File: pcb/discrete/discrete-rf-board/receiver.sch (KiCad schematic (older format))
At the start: 31 parts, among them U7 MAX1193

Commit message: Autofill
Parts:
- C114, C116: footprint (none) -> Capacitor_SMD:C_0402_1005Metric; Mouser (none) -> 80-C0402C104M4P
- R81, R82, R83, R84: footprint (none) -> Resistor_SMD:R_0402_1005Metric; Mouser (none) -> 603-AC0402FR-1310KL
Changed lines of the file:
@@
 F 0 "R82" H 7580 3870 50  0000 L CNN
 F 1 "10kR" H 7580 3810 50  0000 L CNN
-F 2 "" H 7550 3850 50  0001 C CNN
+F 2 "Resistor_SMD:R_0402_1005Metric" H 7550 3850 50  0001 C CNN
 F 3 "~" H 7550 3850 50  0001 C CNN
+F 4 "603-AC0402FR-1310KL" H 7550 3850 50  0001 C CNN "Mouser"
 	1    7550 3850
 	1    0    0    -1
@@
 F 0 "R84" H 7980 3870 50  0000 L CNN
 F 1 "10kR" H 7980 3810 50  0000 L CNN
-F 2 "" H 7950 3850 50  0001 C CNN
+F 2 "Resistor_SMD:R_0402_1005Metric" H 7950 3850 50  0001 C CNN
 F 3 "~" H 7950 3850 50  0001 C CNN
+F 4 "603-AC0402FR-1310KL" H 7950 3850 50  0001 C CNN "Mouser"
 	1    7950 3850
 	1    0    0    -1
@@
 F 0 "R81" H 7580 2470 50  0000 L CNN
 F 1 "10kR" H 7580 2410 50  0000 L CNN
-F 2 "" H 7550 2450 50  0001 C CNN
+F 2 "Resistor_SMD:R_0402_1005Metric" H 7550 2450 50  0001 C CNN
 F 3 "~" H 7550 2450 50  0001 C CNN
+F 4 "603-AC0402FR-1310KL" H 7550 2450 50  0001 C CNN "Mouser"
 	1    7550 2450
 	1    0    0    -1
@@
 F 0 "R83" H 7980 2470 50  0000 L CNN
 F 1 "10kR" H 7980 2410 50  0000 L CNN
-F 2 "" H 7950 2450 50  0001 C CNN
+F 2 "Resistor_SMD:R_0402_1005Metric" H 7950 2450 50  0001 C CNN
 F 3 "~" H 7950 2450 50  0001 C CNN
+F 4 "603-AC0402FR-1310KL" H 7950 2450 50  0001 C CNN "Mouser"
 	1    7950 2450
 	1    0    0    -1
@@
 F 0 "C116" H 10160 2720 50  0000 L CNN
 F 1 "0.1 uF" H 10160 2570 50  0000 L CNN
-F 2 "" H 10150 2650 50  0001 C CNN
+F 2 "Capacitor_SMD:C_0402_1005Metric" H 10150 2650 50  0001 C CNN
 F 3 "~" H 10150 2650 50  0001 C CNN
+F 4 "80-C0402C104M4P" H 10150 2650 50  0001 C CNN "Mouser"
 	1    10150 2650
 	1    0    0    -1
@@
 F 0 "C114" H 9160 2720 50  0000 L CNN
 F 1 "0.1 uF" H 9160 2570 50  0000 L CNN
-F 2 "" H 9150 2650 50  0001 C CNN
+F 2 "Capacitor_SMD:C_0402_1005Metric" H 9150 2650 50  0001 C CNN
 F 3 "~" H 9150 2650 50  0001 C CNN
+F 4 "80-C0402C104M4P" H 9150 2650 50  0001 C CNN "Mouser"
 	1    9150 2650
 	1    0    0    -1

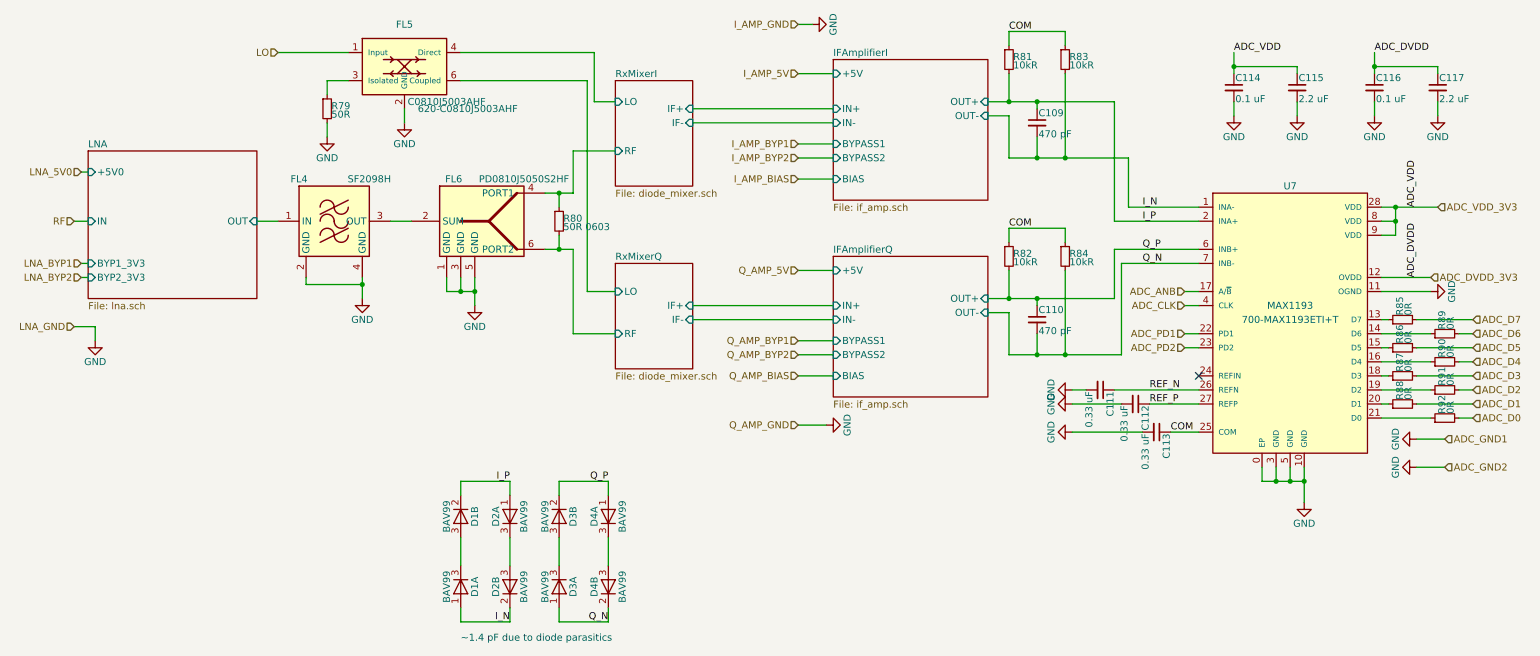
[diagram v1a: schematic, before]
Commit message: Reannotate everything; I'm trying to cut down the number of components
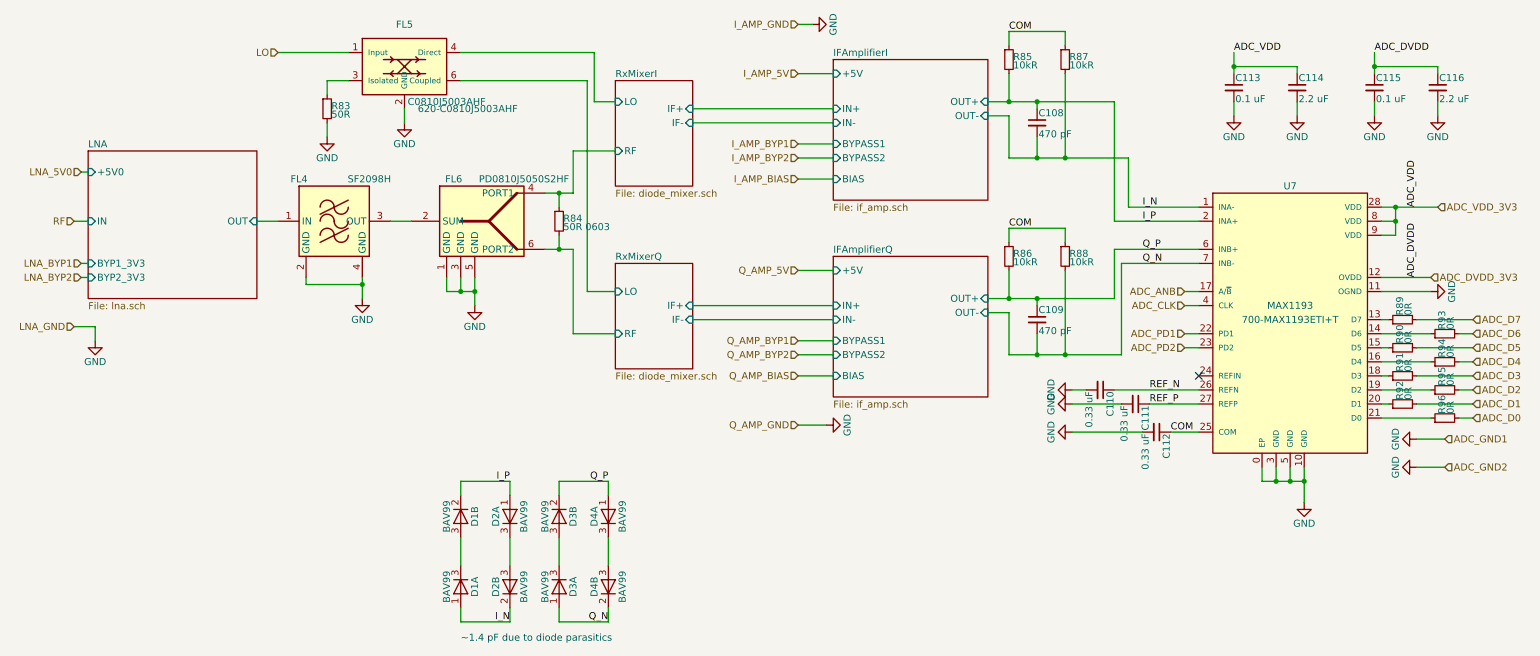
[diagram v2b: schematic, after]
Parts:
- renumbered C109 to C108, C110 to C109, C111 to C110, C112 to C111, C113 to C112, C114 to C113, C115 to C114, C116 to C115, C117 to C116, R79 to R83, R80 to R84, R81 to R85, R82 to R86, R83 to R87, R84 to R88, R85 to R89, R86 to R90, R87 to R91, R88 to R92, R89 to R93, R90 to R94, R91 to R95, R92 to R96

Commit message: Footprint a lot of stuff; save before autofill
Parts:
- C114: footprint (none) -> Capacitor_SMD:C_0402_1005Metric; Mouser (none) -> 963-LMK105BJ225KV-F
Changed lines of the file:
@@
 F 0 "C114" H 9610 2720 50  0000 L CNN
 F 1 "2.2 uF" H 9610 2570 50  0000 L CNN
-F 2 "" H 9600 2650 50  0001 C CNN
+F 2 "Capacitor_SMD:C_0402_1005Metric" H 9600 2650 50  0001 C CNN
 F 3 "~" H 9600 2650 50  0001 C CNN
+F 4 "963-LMK105BJ225KV-F" H 9600 2650 50  0001 C CNN "Mouser"
 	1    9600 2650
 	1    0    0    -1

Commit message: Autofill
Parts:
- C116: footprint (none) -> Capacitor_SMD:C_0402_1005Metric; Mouser (none) -> 963-LMK105BJ225KV-F
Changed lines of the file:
@@
 F 0 "C116" H 10610 2720 50  0000 L CNN
 F 1 "2.2 uF" H 10610 2570 50  0000 L CNN
-F 2 "" H 10600 2650 50  0001 C CNN
+F 2 "Capacitor_SMD:C_0402_1005Metric" H 10600 2650 50  0001 C CNN
 F 3 "~" H 10600 2650 50  0001 C CNN
+F 4 "963-LMK105BJ225KV-F" H 10600 2650 50  0001 C CNN "Mouser"
 	1    10600 2650
 	1    0    0    -1

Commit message: Add in a couple more components, save before autofill
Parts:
- C109: footprint (none) -> Capacitor_SMD:C_0402_1005Metric; Mouser (none) -> 81-GCM155R71H471K37D
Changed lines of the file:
@@
 F 0 "C109" H 7760 4370 50  0000 L CNN
 F 1 "470 pF" H 7760 4220 50  0000 L CNN
-F 2 "" H 7750 4300 50  0001 C CNN
+F 2 "Capacitor_SMD:C_0402_1005Metric" H 7750 4300 50  0001 C CNN
 F 3 "~" H 7750 4300 50  0001 C CNN
+F 4 "81-GCM155R71H471K37D" H 7750 4300 50  0001 C CNN "Mouser"
 	1    7750 4300
 	1    0    0    -1

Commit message: Autofill
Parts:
- C108: footprint (none) -> Capacitor_SMD:C_0402_1005Metric; Mouser (none) -> 81-GCM155R71H471K37D
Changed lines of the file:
@@
 F 0 "C108" H 7760 2970 50  0000 L CNN
 F 1 "470 pF" H 7760 2820 50  0000 L CNN
-F 2 "" H 7750 2900 50  0001 C CNN
+F 2 "Capacitor_SMD:C_0402_1005Metric" H 7750 2900 50  0001 C CNN
 F 3 "~" H 7750 2900 50  0001 C CNN
+F 4 "81-GCM155R71H471K37D" H 7750 2900 50  0001 C CNN "Mouser"
 	1    7750 2900
 	1    0    0    -1

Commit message: Footprint more stuff
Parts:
- R84: value 50R 0603 -> 51R 0603
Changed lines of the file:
@@
 P 4350 3600
 F 0 "R84" H 4380 3620 50  0000 L CNN
-F 1 "50R 0603" H 4380 3560 50  0000 L CNN
+F 1 "51R 0603" H 4380 3560 50  0000 L CNN
 F 2 "" H 4350 3600 50  0001 C CNN
 F 3 "~" H 4350 3600 50  0001 C CNN

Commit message: Autofill
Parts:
- R83: footprint (none) -> Resistor_SMD:R_0402_1005Metric; Mouser (none) -> 603-RC0402JR-0750RL
- R84: footprint (none) -> Resistor_SMD:R_0603_1608Metric_Pad1.05x0.95mm_HandSolder; Mouser (none) -> 603-RC0603FR-0751RL
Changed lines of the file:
@@
 F 0 "R83" H 2730 2820 50  0000 L CNN
 F 1 "50R" H 2730 2760 50  0000 L CNN
-F 2 "" H 2700 2800 50  0001 C CNN
+F 2 "Resistor_SMD:R_0402_1005Metric" H 2700 2800 50  0001 C CNN
 F 3 "~" H 2700 2800 50  0001 C CNN
+F 4 "603-RC0402JR-0750RL" H 2700 2800 50  0001 C CNN "Mouser"
 	1    2700 2800
 	1    0    0    -1
@@
 F 0 "R84" H 4380 3620 50  0000 L CNN
 F 1 "51R 0603" H 4380 3560 50  0000 L CNN
-F 2 "" H 4350 3600 50  0001 C CNN
+F 2 "Resistor_SMD:R_0603_1608Metric_Pad1.05x0.95mm_HandSolder" H 4350 3600 50  0001 C CNN
 F 3 "~" H 4350 3600 50  0001 C CNN
+F 4 "603-RC0603FR-0751RL" H 4350 3600 50  0001 C CNN "Mouser"
 	1    4350 3600
 	1    0    0    -1
